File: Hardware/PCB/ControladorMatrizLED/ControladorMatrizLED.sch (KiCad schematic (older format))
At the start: 13 parts

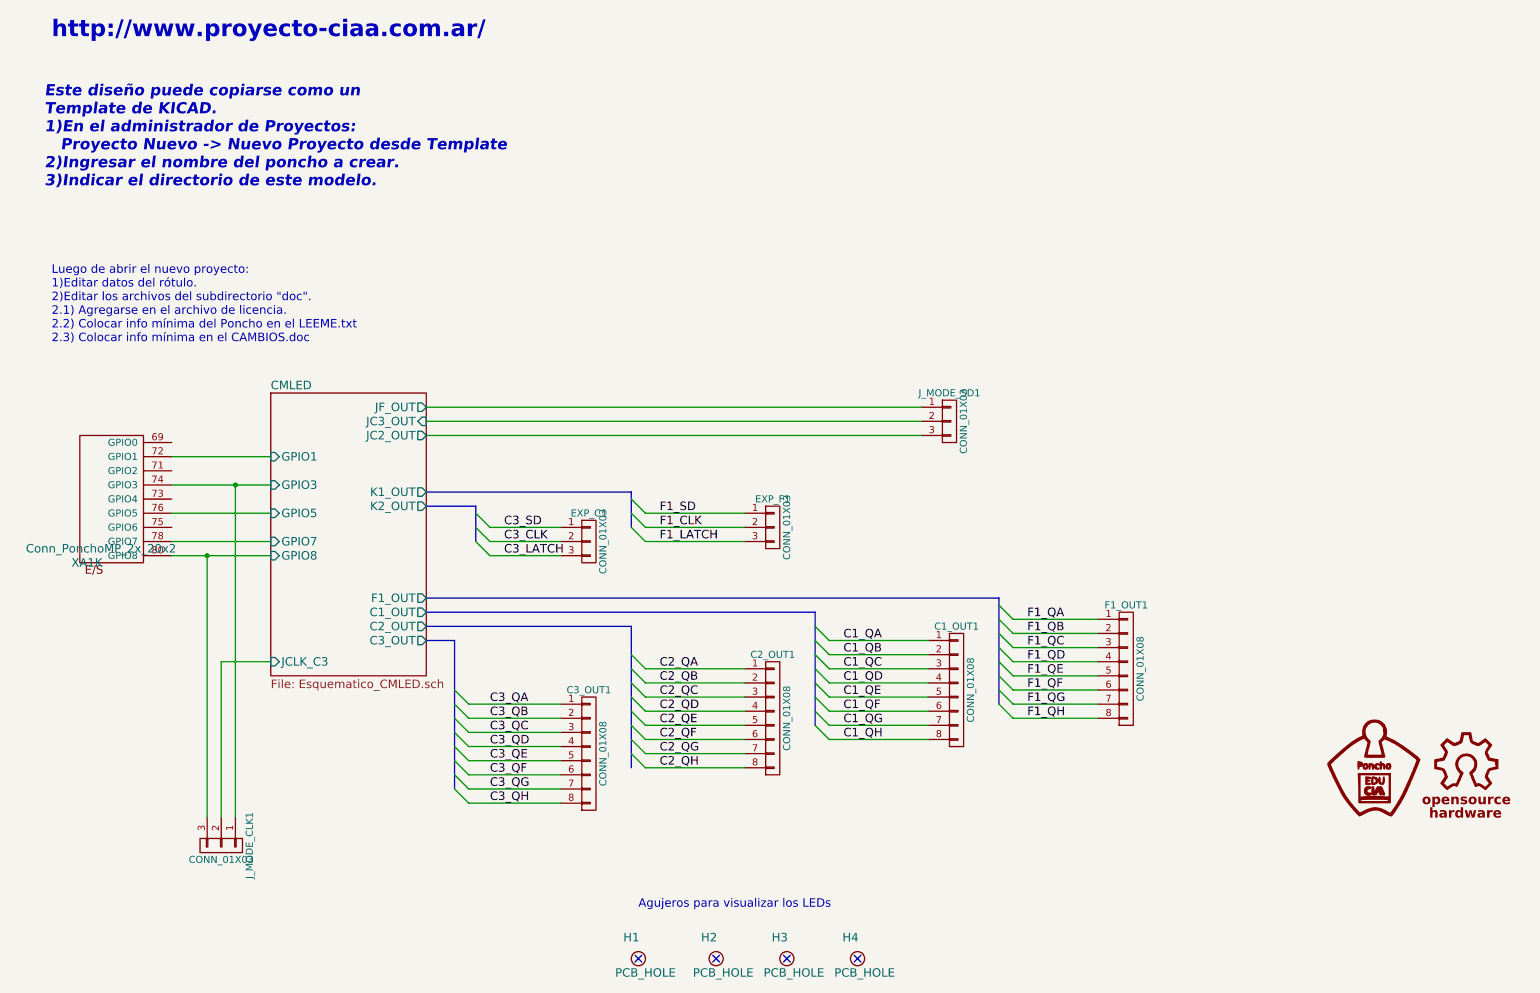
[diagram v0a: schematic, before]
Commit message: Avance sobre Esquematico y PCB - Pistas terminadas
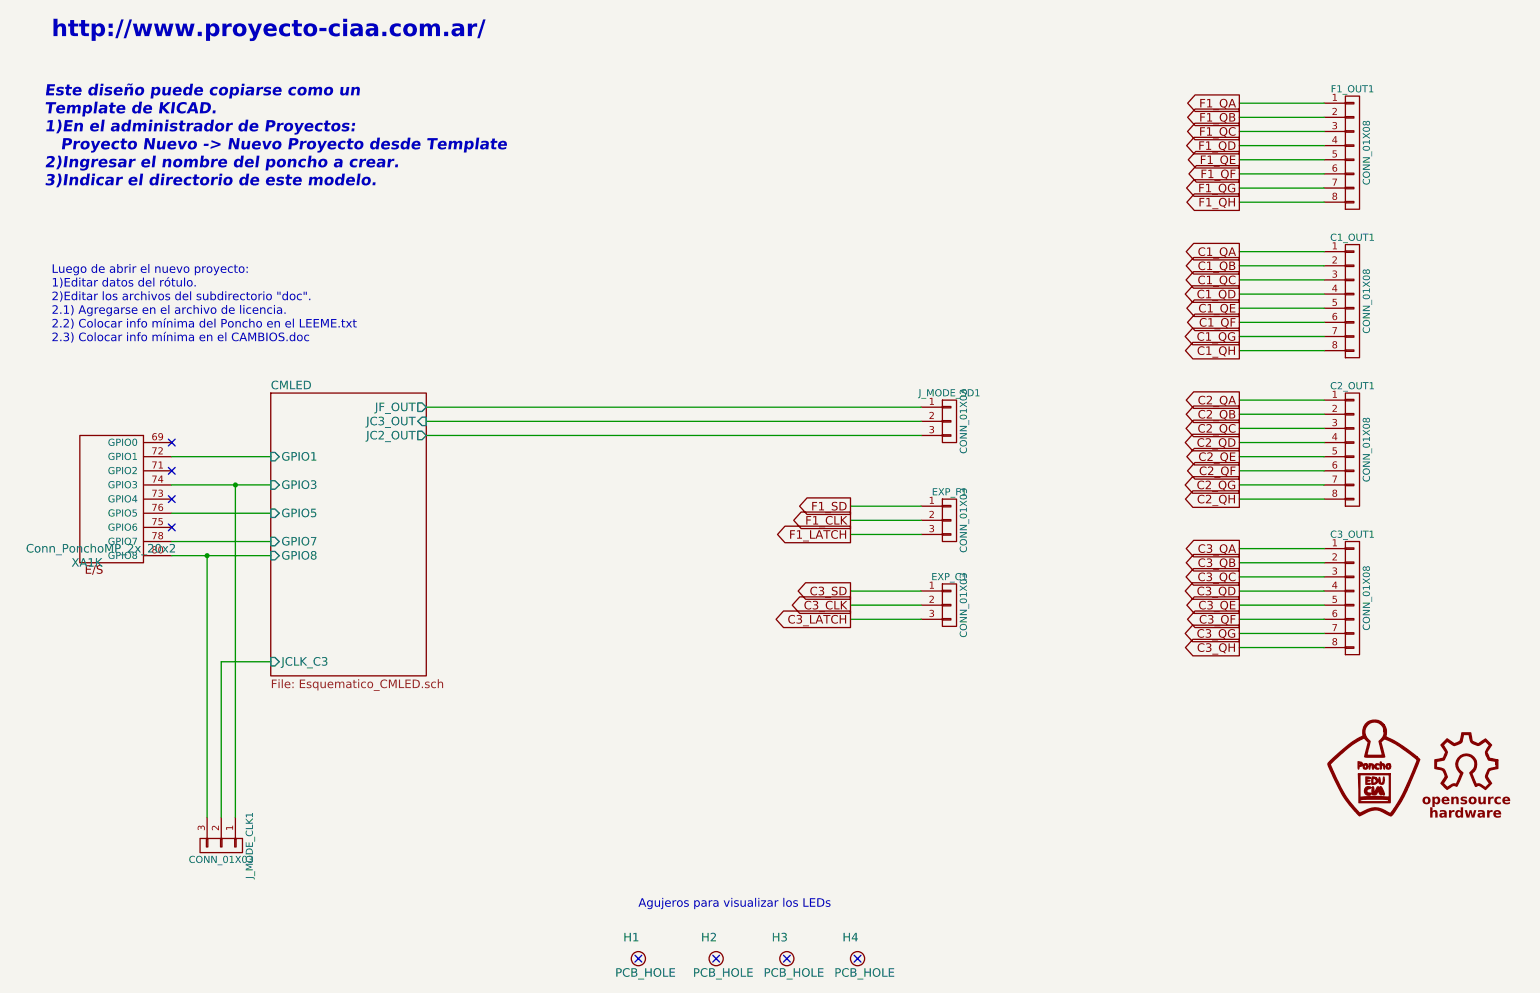
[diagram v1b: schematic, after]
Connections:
- no-connect marks 4 -> 8
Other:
- moved on the sheet: C1_OUT1, C2_OUT1, C3_OUT1, EXP_C1, EXP_F1, F1_OUT1

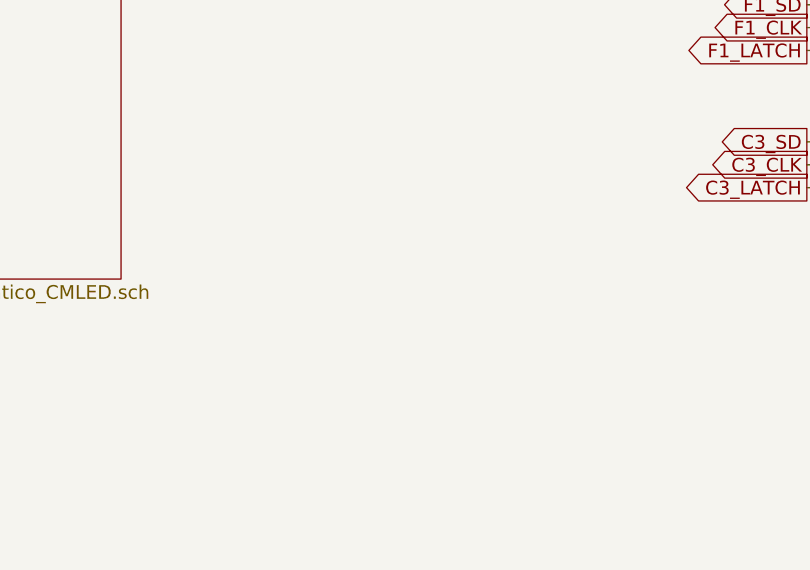
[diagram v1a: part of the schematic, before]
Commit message: Pistas completas y prueba de impreso añadida
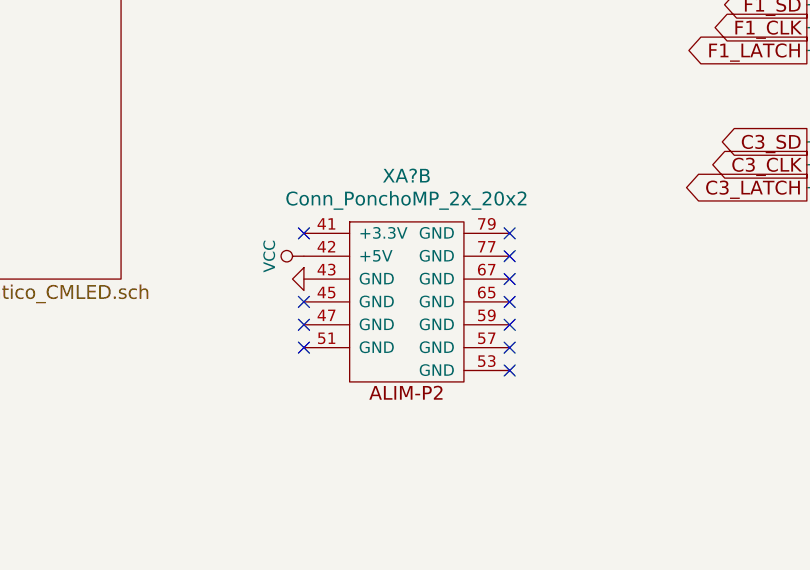
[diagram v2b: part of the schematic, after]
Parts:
- added XA?: Conn_PonchoMP_2x_20x2, symbol Conn_PonchoMP_2x_20x2
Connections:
- new net GND: XA?.43 (GND)
- new net VCC: XA?.42 (+5V)
- no-connect marks 8 -> 19
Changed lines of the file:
@@
 NoConn ~ 1650 4100
 NoConn ~ 1650 4300
+$Comp
+L Conn_PonchoMP_2x_20x2 XA?
+U 2 1 5658B4BB
+P 4700 5450
+F 0 "XA?" H 4700 6000 60  0000 C CNN
+F 1 "Conn_PonchoMP_2x_20x2" H 4700 5900 60  0000 C CNN
+F 2 "" H 4550 5800 60  0000 C CNN
+F 3 "" H 4550 5800 60  0000 C CNN
+	2    4700 5450
+	1    0    0    -1
+$EndComp
+$Comp
+L GND #PWR?
+U 1 1 56588A59
+P 4250 5350
+F 0 "#PWR?" H 4250 5350 30  0001 C CNN
+F 1 "GND" H 4250 5280 30  0001 C CNN
+F 2 "" H 4250 5350 60  0000 C CNN
+F 3 "" H 4250 5350 60  0000 C CNN
+	1    4250 5350
+	0    1    1    0
+$EndComp
+$Comp
+L VCC #PWR?
+U 1 1 56588C71
+P 4250 5250
+F 0 "#PWR?" H 4250 5100 50  0001 C CNN
+F 1 "VCC" H 4250 5400 50  0000 C CNN
+F 2 "" H 4250 5250 60  0000 C CNN
+F 3 "" H 4250 5250 60  0000 C CNN
+	1    4250 5250
+	0    -1   -1   0
+$EndComp
+NoConn ~ 4250 5150
+NoConn ~ 4250 5450
+NoConn ~ 4250 5550
+NoConn ~ 4250 5650
+NoConn ~ 5150 5750
+NoConn ~ 5150 5650
+NoConn ~ 5150 5550
+NoConn ~ 5150 5450
+NoConn ~ 5150 5350
+NoConn ~ 5150 5250
+NoConn ~ 5150 5150
 $EndSCHEMATC

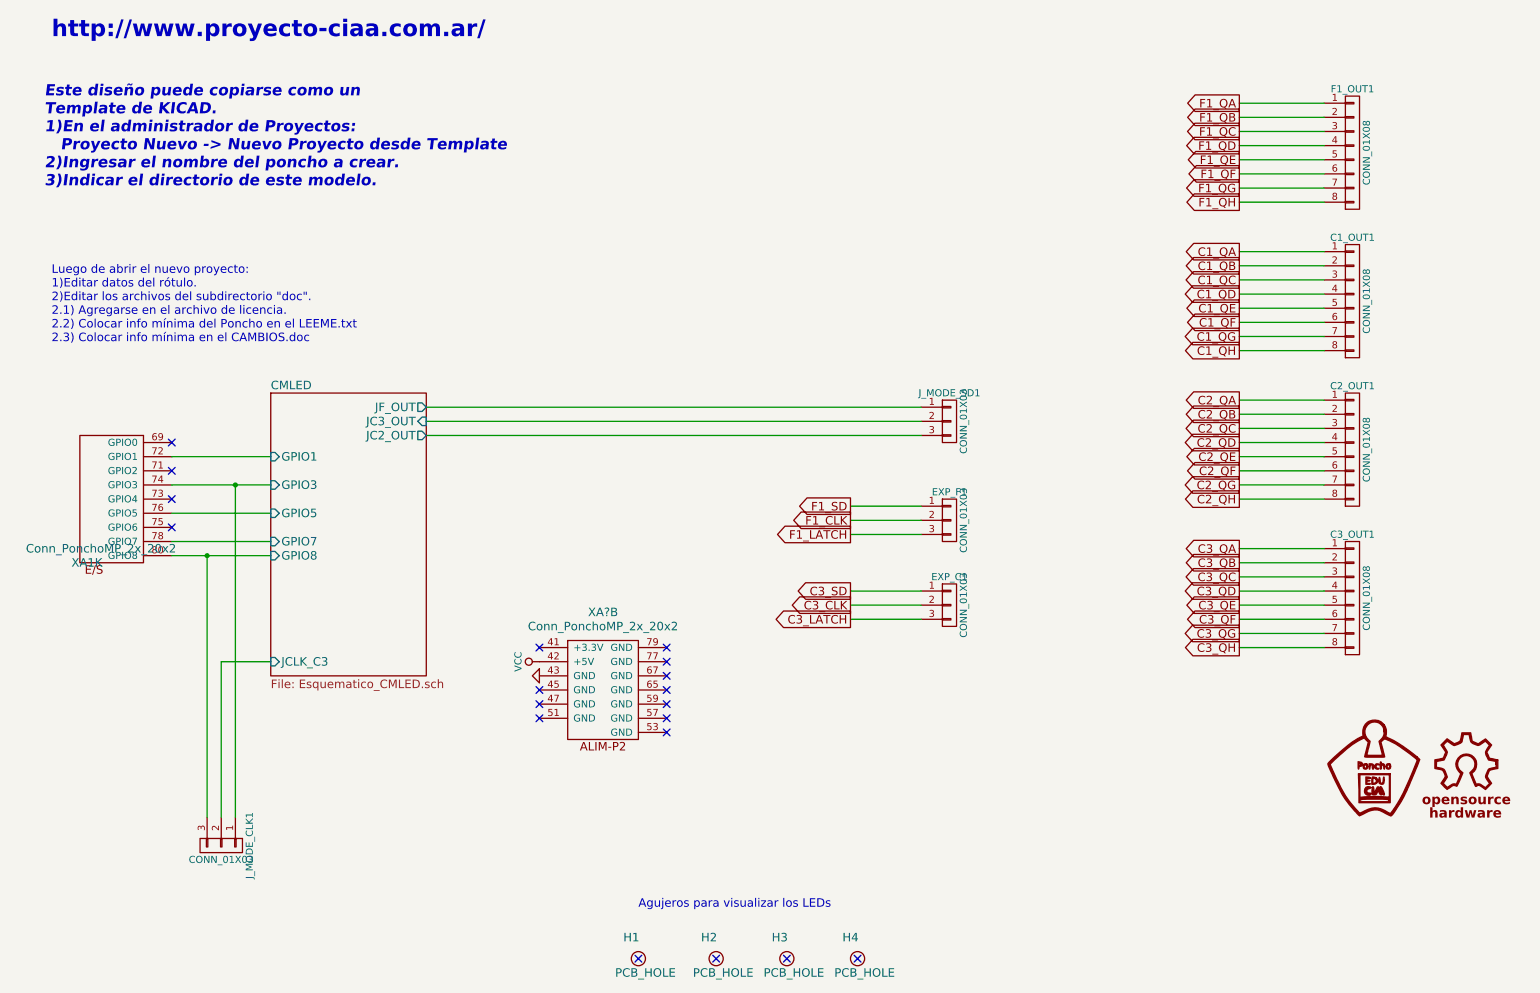
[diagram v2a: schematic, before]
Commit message: Actualizacion con modelo poncho grande y LCD
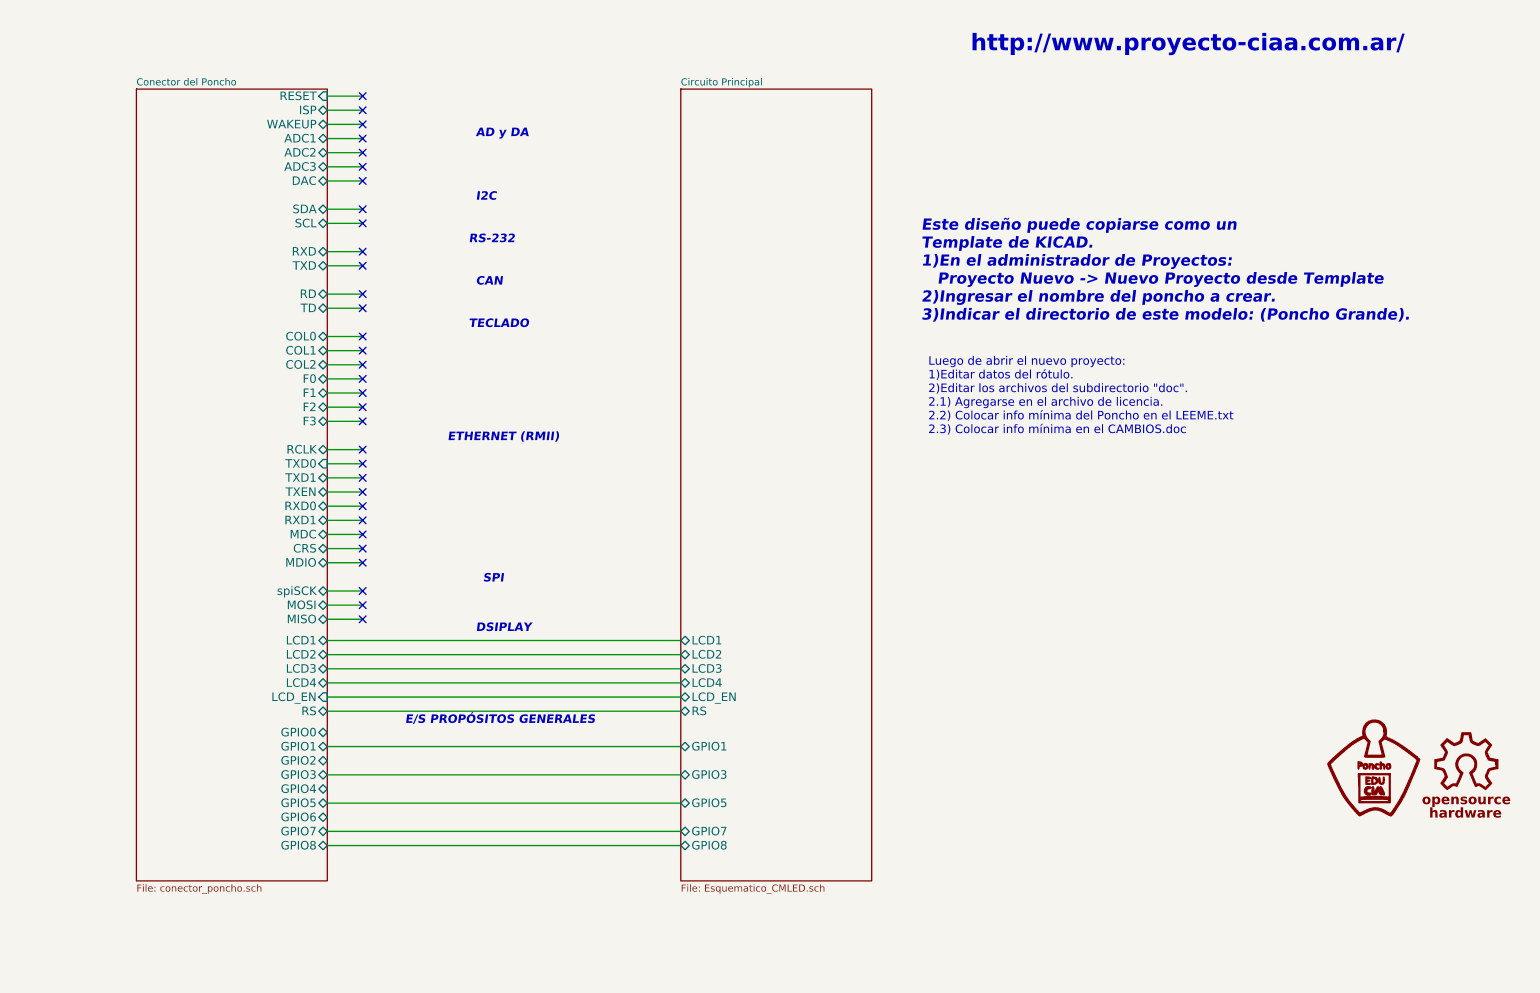
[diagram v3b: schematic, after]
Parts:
- removed C1_OUT1, C2_OUT1, C3_OUT1, F1_OUT1: CONN_01X08, Pin_Headers:Pin_Header_Straight_1x08, symbol CONN_01X08
- removed EXP_C1, EXP_F1, J_MODE_CLK1, J_MODE_SD1: CONN_01X03, Pin_Headers:Pin_Header_Straight_1x03, symbol CONN_01X03
- removed H1, H2, H3, H4: PCB_HOLE, Poncho_Modelos:Led_Hole, symbol PCB_HOLE
- removed XA1: Conn_PonchoMP_2x_20x2, Poncho_Esqueleto:Conn_Poncho_Mediano, symbol Conn_PonchoMP_2x_20x2
- removed XA?: Conn_PonchoMP_2x_20x2, symbol Conn_PonchoMP_2x_20x2
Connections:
- no-connect marks 19 -> 32
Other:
- note added: "AD y DA"
- note added: "CAN"
- note added: "DSIPLAY"
- note added: "E/S PROPÓSITOS GENERALES"
- note added: "ETHERNET (RMII)"
- note added: "Este diseño puede copiarse como un \nTemplate de KICAD. \n1)En el administrador de Proyectos: \n Proyecto Nuevo -> Nuevo Proyecto desde Template\n2)Ingresar el nombre del poncho a crear.\n3)Indicar el directorio de este modelo: (Poncho Grande)."
- note added: "I2C"
- note added: "RS-232"
- note added: "SPI"
- note added: "TECLADO"
- note removed: "Agujeros para visualizar los LEDs"
- note removed: "Este diseño puede copiarse como un \nTemplate de KICAD. \n1)En el administrador de Proyectos: \n Proyecto Nuevo -> Nuevo Proyecto desde Template\n2)Ingresar el nombre del poncho a crear.\n3)Indicar el directorio de este modelo."
